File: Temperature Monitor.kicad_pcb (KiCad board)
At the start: 2 copper layers, 60 x 60 mm, 11 parts, among them J1 Battery, J2 BME 280, J3 Display, SW1 Up, SW2 Down, SW3 Select, U2 XIAO-ESP32-C6-SMD

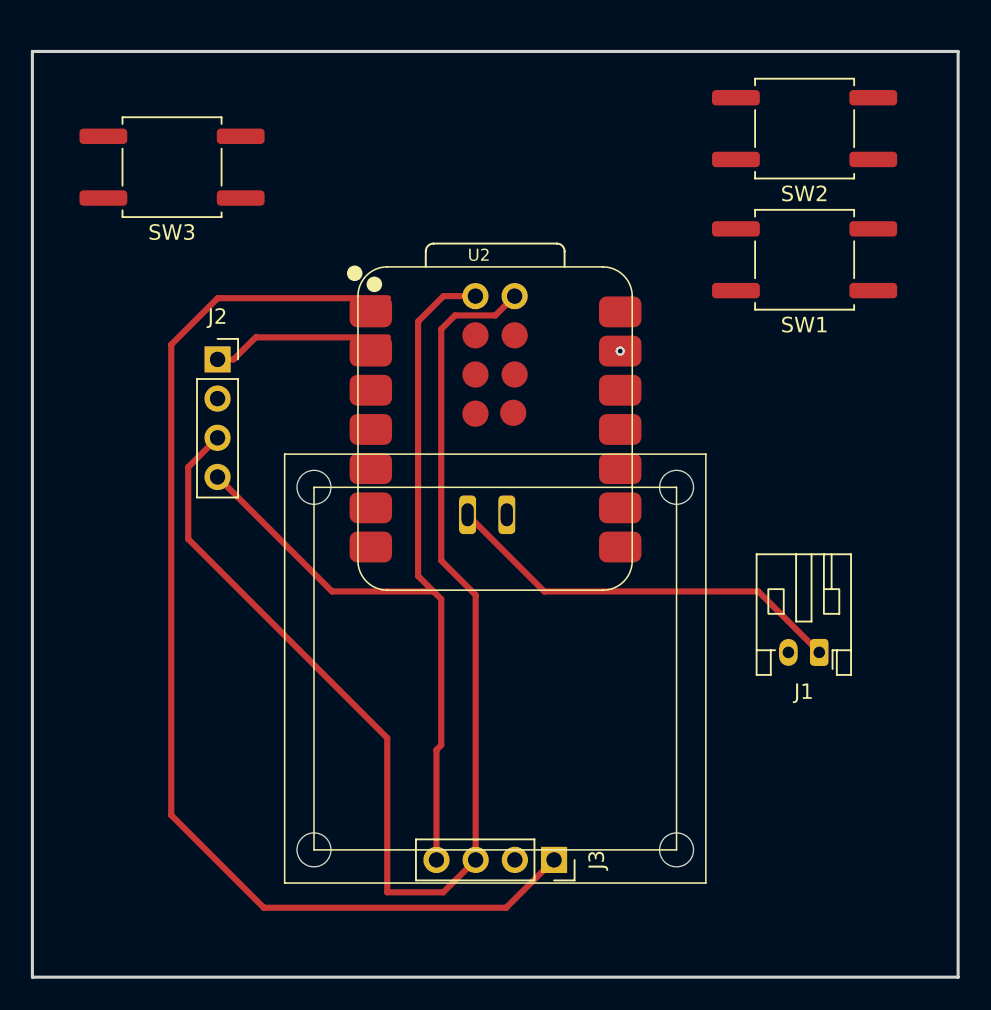
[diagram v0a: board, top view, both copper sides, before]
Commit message: Added buttons
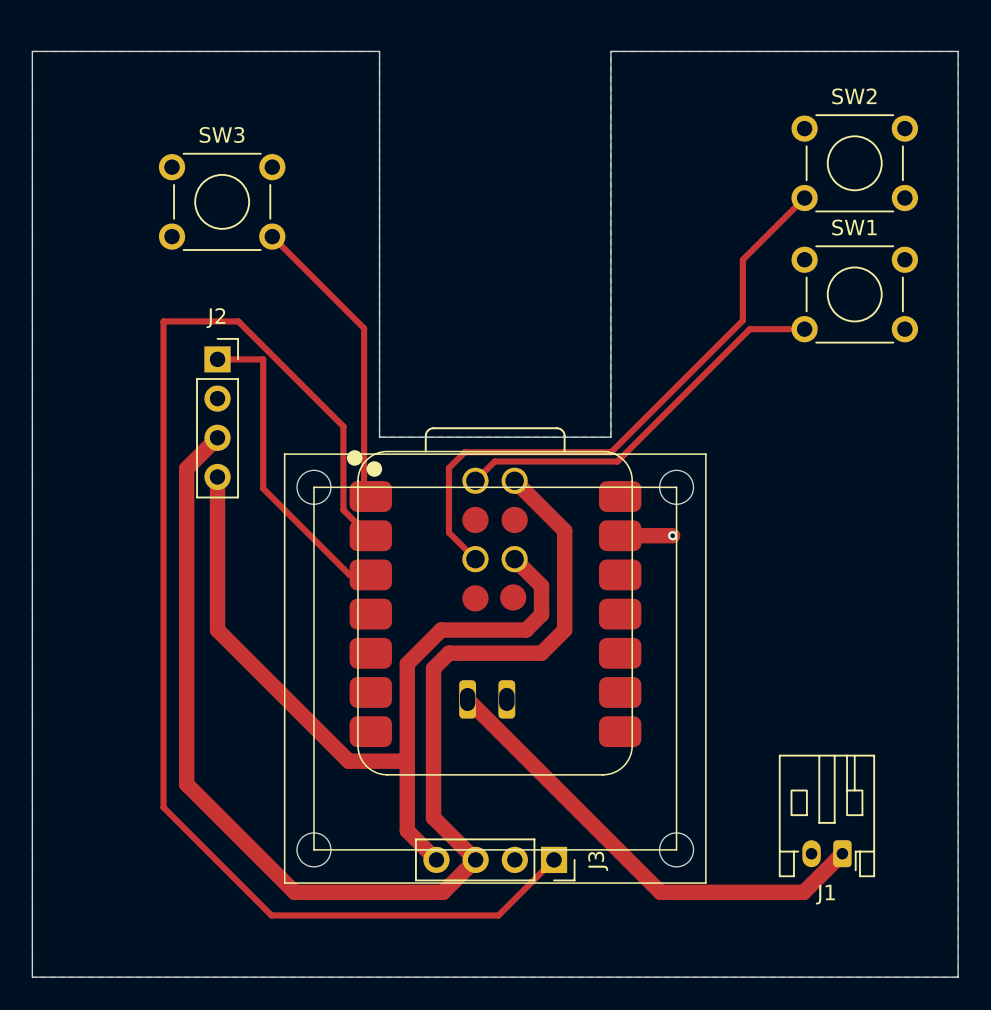
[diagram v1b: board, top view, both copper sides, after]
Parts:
- SW1: footprint Button_Switch_SMD:SW_Push_1P1T_NO_CK_KSC6xxG -> Button_Switch_THT:SW_TH_Tactile_Omron_B3F-100x
- SW2: footprint Button_Switch_SMD:SW_Push_1P1T_NO_CK_KSC6xxG -> Button_Switch_THT:SW_TH_Tactile_Omron_B3F-102x
- SW3: footprint Button_Switch_SMD:SW_Push_1P1T_NO_CK_KSC6xxG -> Button_Switch_THT:SW_TH_Tactile_Omron_B3F-106x
- moved J1 13.1 mm to (162.5, 127.0)
- moved U2 12.0 mm to (131.1, 122.0)
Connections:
- net Net-(J1-Pin_1) renamed /VBAT
- net Net-(J2-Pin_3) renamed /SCL
- J2 pad 1: Net-(J2-Pin_1) -> /SENS_PWR
- J2 pad 4: Net-(J2-Pin_4) -> /SDA
- J3 pad 1: Net-(J3-Pin_1) -> /DISP_PWR
- J3 pad 4: Net-(J2-Pin_4) -> /SDA
- SW1 pad 1: unconnected-(SW1-Pad1) -> GND
- SW1 pad 2: unconnected-(SW1-Pad2) -> Net-(U2-MTDI)
- SW2 pad 1: unconnected-(SW2-Pad1) -> GND
- SW2 pad 2: unconnected-(SW2-Pad2) -> Net-(U2-MTMS)
- SW3 pad 1: unconnected-(SW3-Pad1) -> GND
- SW3 pad 2: unconnected-(SW3-Pad2) -> Net-(U2-D0)
- U2 pad 1: Net-(J3-Pin_1) -> Net-(U2-D0)
- U2 pad 15: Net-(J2-Pin_4) -> Net-(U2-MTDI)
- U2 pad 19: unconnected-(U2-MTMS-Pad19) -> Net-(U2-MTMS)
- U2 pad 2: Net-(J2-Pin_1) -> /DISP_PWR
- U2 pad 20: unconnected-(U2-MTCK-Pad20) -> /SDA
- U2 pad 3: unconnected-(U2-D2-Pad3) -> /SENS_PWR
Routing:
- net /DISP_PWR: track 0.00 -> 83.7 mm
- net Net-(J3-Pin_1): track 74.4 -> 0.00 mm
- net Net-(J2-Pin_4): track 57.1 -> 0.00 mm
- net /SDA: track 0.00 -> 53.6 mm
- net Net-(U2-MTMS): track 0.00 -> 39.2 mm
- net Net-(U2-MTDI): track 0.00 -> 25.4 mm
- net /SENS_PWR: track 0.00 -> 20.6 mm
- net Net-(U2-D0): track 0.00 -> 20.2 mm
- net Net-(J2-Pin_1): track 11.7 -> 0.00 mm
- net /VBAT: track 26.5 -> 30.5 mm
- net GND: track 0.00 -> 3.40 mm
- net /SCL: track 83.2 -> 79.9 mm
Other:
- outline, holes or cut-outs redrawn

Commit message: Added SCL resistor
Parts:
- added R1: 220R, Resistor_THT:R_Axial_DIN0207_L6.3mm_D2.5mm_P7.62mm_Horizontal, F.Cu at (131.1, 123.5)
- added R2: 220R, Resistor_THT:R_Axial_DIN0207_L6.3mm_D2.5mm_P7.62mm_Horizontal, F.Cu at (125.0, 109.0)
- added R3: 5K, Resistor_THT:R_Axial_DIN0207_L6.3mm_D2.5mm_P7.62mm_Horizontal, F.Cu at (148.5, 123.5)
- moved J2 7.18 mm to (126.0, 89.0)
- moved SW3 3.59 mm to (116.8, 79.8)
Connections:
- U2 pad 12: unconnected-(U2-3V3_OUT-Pad12) -> /SENS_PWR
- U2 pad 3: /SENS_PWR -> Net-(U2-D2)
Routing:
- net /SDA: track 53.6 -> 82.1 mm
- net Net-(U2-D2): track 0.00 -> 22.7 mm
- net /SCL: track 79.9 -> 98.4 mm
- net /DISP_PWR: track 83.7 -> 73.9 mm
- net /VBAT: track 30.5 -> 38.8 mm
- net Net-(U2-MTDI): track 25.4 -> 29.8 mm
- net /SENS_PWR: track 20.6 -> 16.7 mm
- net Net-(U2-D0): track 20.2 -> 23.9 mm
- net Net-(U2-MTMS): track 39.2 -> 42.2 mm

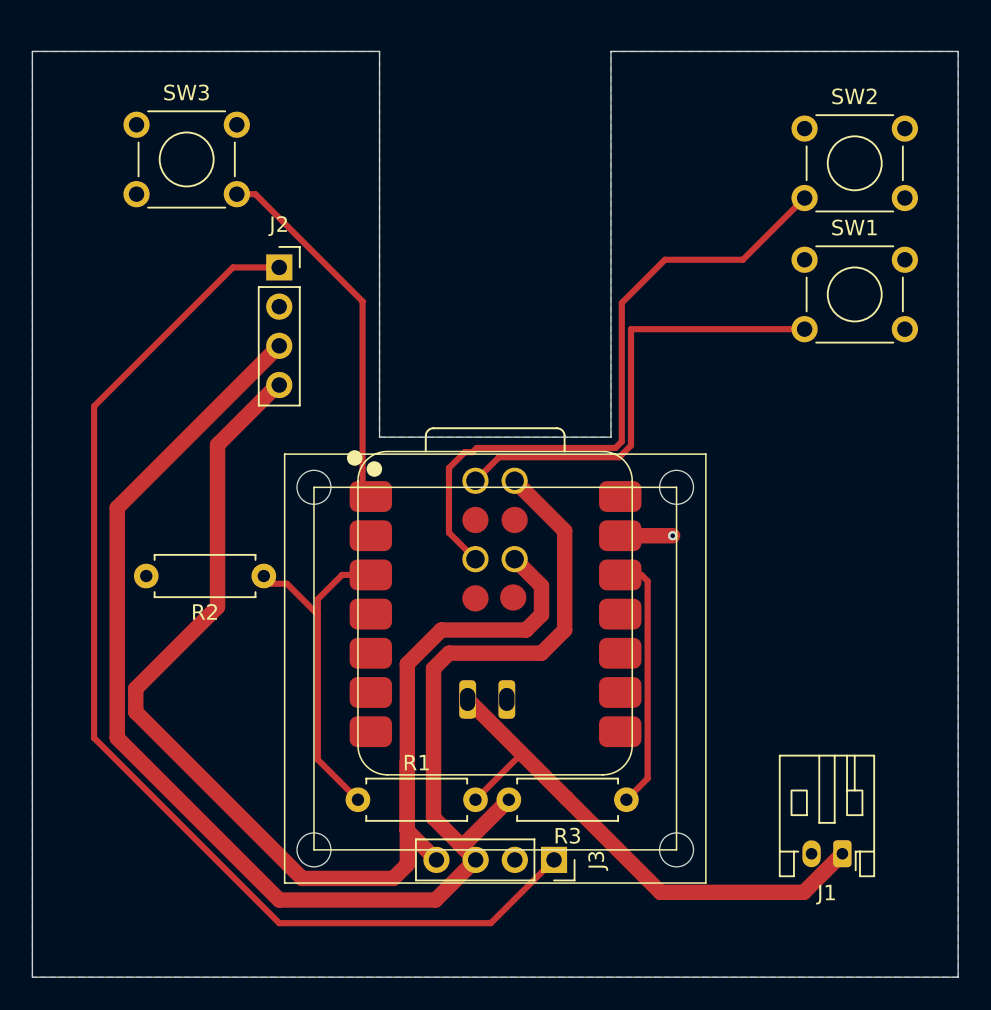
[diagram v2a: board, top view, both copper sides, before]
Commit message: Added Underside Traces
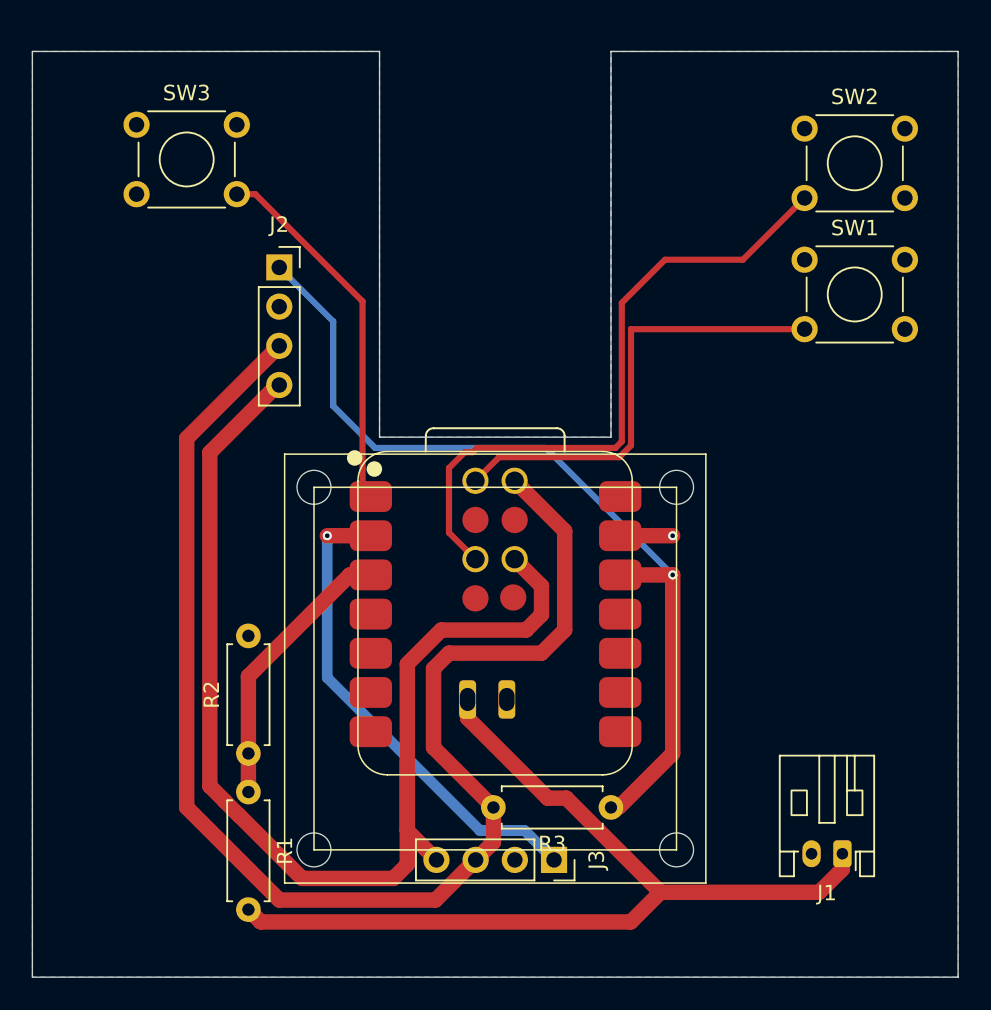
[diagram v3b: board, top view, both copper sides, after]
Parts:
- moved R2 11.5 mm to (124.0, 120.5), turned to 90 degrees
- moved R1 7.12 mm to (124.0, 123.0), turned to -90 degrees
- moved R3 1.12 mm to (147.5, 124.0)
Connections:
- net Net-(U2-D2) renamed /BATT_V
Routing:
- net /DISP_PWR: track 73.9 -> 31.8 mm, vias 0 -> 1
- net /SENS_PWR: track 16.7 -> 57.4 mm, vias 0 -> 1
- net /VBAT: track 38.8 -> 62.9 mm
- net /SCL: track 98.4 -> 89.7 mm
- net /BATT_V: track 22.7 -> 18.2 mm
- net /SDA: track 82.1 -> 78.1 mm

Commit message: Updated to match SMB circuit
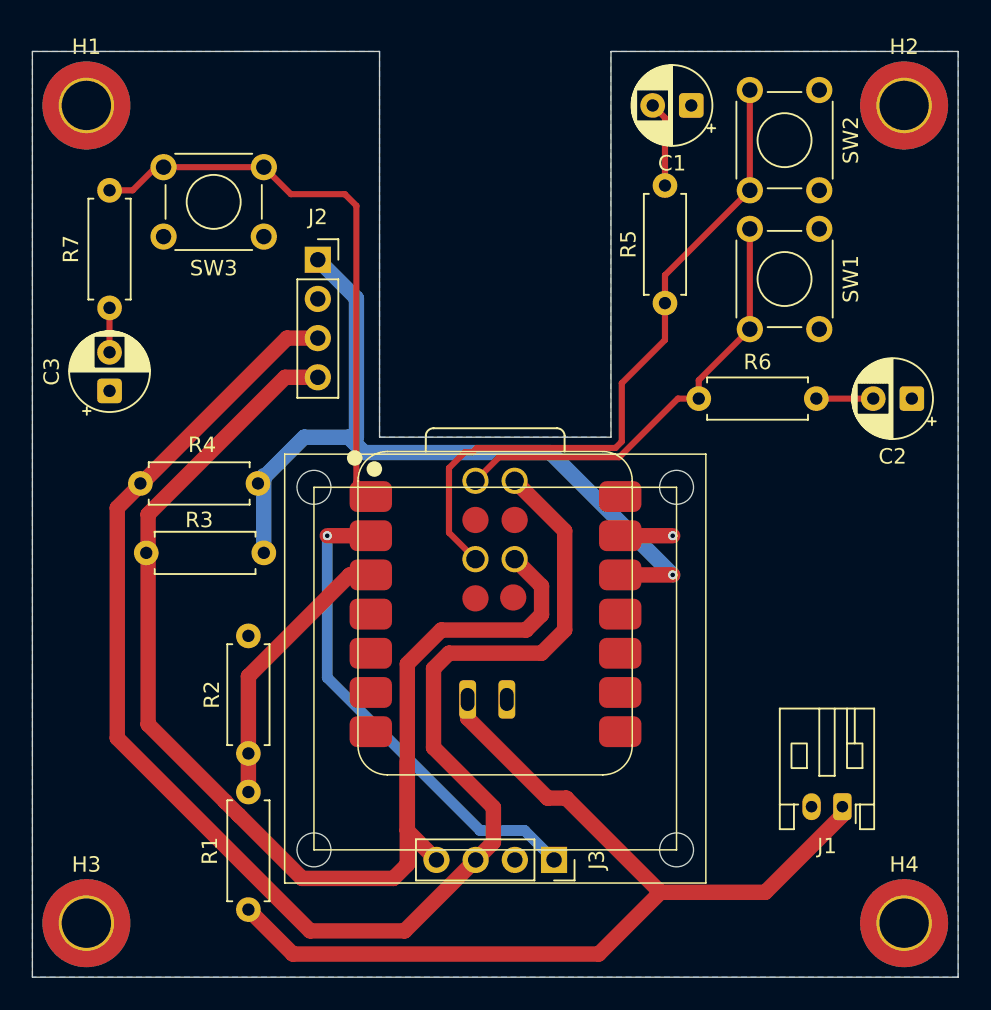
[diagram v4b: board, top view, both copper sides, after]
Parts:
- added C1: 0.1, Capacitor_THT:CP_Radial_D5.0mm_P2.50mm, F.Cu at (152.7, 78.5)
- added C2: 0.1, Capacitor_THT:CP_Radial_D5.0mm_P2.50mm, F.Cu at (167.0, 97.5)
- added C3: 0.1, Capacitor_THT:CP_Radial_D5.0mm_P2.50mm, F.Cu at (115.0, 97.0)
- added H1: MountingHole_Pad, MountingHole:MountingHole_3.2mm_M3_ISO7380_Pad_TopBottom, F.Cu at (113.5, 78.5)
- added H2: MountingHole_Pad, MountingHole:MountingHole_3.2mm_M3_ISO7380_Pad_TopBottom, F.Cu at (166.5, 78.5)
- added H3: MountingHole_Pad, MountingHole:MountingHole_3.2mm_M3_ISO7380_Pad_TopBottom, F.Cu at (113.5, 131.5)
- added H4: MountingHole_Pad, MountingHole:MountingHole_3.2mm_M3_ISO7380_Pad_TopBottom, F.Cu at (166.5, 131.5)
- added R4: 5K, Resistor_THT:R_Axial_DIN0207_L6.3mm_D2.5mm_P7.62mm_Horizontal, F.Cu at (117.4, 107.5)
- added R5: 1K, Resistor_THT:R_Axial_DIN0207_L6.3mm_D2.5mm_P7.62mm_Horizontal, F.Cu at (151.0, 91.3)
- added R6: 1K, Resistor_THT:R_Axial_DIN0207_L6.3mm_D2.5mm_P7.62mm_Horizontal, F.Cu at (153.2, 97.5)
- added R7: 1K, Resistor_THT:R_Axial_DIN0207_L6.3mm_D2.5mm_P7.62mm_Horizontal, F.Cu at (115.0, 84.0)
- moved R3 31.1 mm to (124.6, 103.0)
- moved SW3 11.0 mm to (125.0, 87.0), turned to 180 degrees
- moved J1 3.05 mm to (162.5, 124.0)
- moved SW2 2.67 mm to (161.0, 77.5), turned to -90 degrees
- moved J2 2.55 mm to (128.5, 88.5)
- moved SW1 2.21 mm to (161.0, 86.5), turned to -90 degrees
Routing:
- net Net-(U2-D0): track 23.9 -> 36.4 mm
- net /SCL: track 89.7 -> 97.8 mm
- net /SDA: track 78.1 -> 84.1 mm
- net Net-(C1-Pad2): track 0.00 -> 5.52 mm
- net /SENS_PWR: track 57.4 -> 53.1 mm
- net Net-(C2-Pad2): track 0.00 -> 3.69 mm
- net Net-(C3-Pad2): track 0.00 -> 2.88 mm
- net Net-(U2-MTMS): track 42.2 -> 44.8 mm
- net Net-(U2-MTDI): track 29.8 -> 29.1 mm
- net /VBAT: track 62.9 -> 62.4 mm

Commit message: General Improvements
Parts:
- C1, C2: value 0.1 -> 0.1U
- R1, R2: value 220R -> 220K
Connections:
- net Net-(U2-MTDI) renamed /Up
- net Net-(U2-MTMS) renamed /Down
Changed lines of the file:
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@@
 			)
 		)
-		(property "Value" "220R"
+		(property "Value" "220K"
 			(at 3.81 2.37 90)
 			(layer "F.Fab")
@@
 			(keep_end_layers yes)
 			(zone_layer_connections)
-			(net "Net-(U2-MTMS)")
+			(net "/Down")
 			(pinfunction "2_2")
 			(pintype "passive")
@@
 			(keep_end_layers yes)
 			(zone_layer_connections)
-			(net "Net-(U2-MTMS)")
+			(net "/Down")
 			(pinfunction "2_2")
 			(pintype "passive")
@@
 			(keep_end_layers yes)
 			(zone_layer_connections)
-			(net "Net-(U2-MTDI)")
+			(net "/Up")
 			(pintype "passive")
 		)
@@
 			)
 		)
-		(property "Value" "0.1"
+		(property "Value" "0.1U"
 			(at 1.25 3.75 0)
 			(layer "F.Fab")
@@
 			(keep_end_layers yes)
 			(zone_layer_connections)
-			(net "Net-(U2-MTDI)")
+			(net "/Up")
 			(pinfunction "MTDI_15")
 			(pintype "passive")
@@
 			(keep_end_layers yes)
 			(zone_layer_connections)
-			(net "Net-(U2-MTMS)")
+			(net "/Down")
 			(pinfunction "MTMS_19")
 			(pintype "passive")
@@
 			(keep_end_layers yes)
 			(zone_layer_connections)
-			(net "Net-(U2-MTMS)")
+			(net "/Down")
 			(pintype "passive")
 		)
@@
 			(keep_end_layers yes)
 			(zone_layer_connections)
-			(net "Net-(U2-MTDI)")
+			(net "/Up")
 			(pinfunction "2_2")
 			(pintype "passive")
@@
 			(keep_end_layers yes)
 			(zone_layer_connections)
-			(net "Net-(U2-MTDI)")
+			(net "/Up")
 			(pinfunction "2_2")
 			(pintype "passive")
@@
 			)
 		)
-		(property "Value" "0.1"
+		(property "Value" "0.1U"
 			(at 1.25 3.75 0)
 			(layer "F.Fab")
@@
 			)
 		)
-		(property "Value" "220R"
+		(property "Value" "220K"
 			(at 3.81 -0.5 90)
 			(layer "F.Fab")
@@
 	)
 	(segment
+		(start 115 91.62)
+		(end 115 94.5)
+		(width 0.4)
+		(layer "F.Cu")
+		(net "Net-(C3-Pad2)")
+	)
+	(segment
 		(start 157.5 129.5)
 		(end 162.5 124.5)
@@
 	)
 	(segment
-		(start 148.2 100.289949)
-		(end 148.2 96.5)
-		(width 0.4)
-		(layer "F.Cu")
-		(net "Net-(U2-MTMS)")
-	)
-	(segment
-		(start 151 91.31)
-		(end 151 93.7)
-		(width 0.4)
-		(layer "F.Cu")
-		(net "Net-(U2-MTMS)")
-	)
-	(segment
-		(start 138.7166 107.9068)
-		(end 137 106.1902)
-		(width 0.4)
-		(layer "F.Cu")
-		(net "Net-(U2-MTMS)")
-	)
-	(segment
-		(start 156.5 84)
-		(end 156.5 77.5)
-		(width 0.4)
-		(layer "F.Cu")
-		(net "Net-(U2-MTMS)")
-	)
-	(segment
-		(start 138.0232 100.9768)
-		(end 138.5232 100.9768)
-		(width 0.4)
-		(layer "F.Cu")
-		(net "Net-(U2-MTMS)")
-	)
-	(segment
-		(start 151 93.7)
-		(end 148.2 96.5)
-		(width 0.4)
-		(layer "F.Cu")
-		(net "Net-(U2-MTMS)")
-	)
-	(segment
-		(start 138.8 100.7)
-		(end 147.789949 100.7)
-		(width 0.4)
-		(layer "F.Cu")
-		(net "Net-(U2-MTMS)")
-	)
-	(segment
-		(start 137 106.1902)
-		(end 137 102)
-		(width 0.4)
-		(layer "F.Cu")
-		(net "Net-(U2-MTMS)")
-	)
-	(segment
-		(start 151 91.31)
-		(end 151 89.5)
-		(width 0.4)
-		(layer "F.Cu")
-		(net "Net-(U2-MTMS)")
-	)
-	(segment
-		(start 137 102)
-		(end 138.0232 100.9768)
-		(width 0.4)
-		(layer "F.Cu")
-		(net "Net-(U2-MTMS)")
-	)
-	(segment
-		(start 138.5232 100.9768)
-		(end 138.8 100.7)
-		(width 0.4)
-		(layer "F.Cu")
-		(net "Net-(U2-MTMS)")
-	)
-	(segment
-		(start 147.789949 100.7)
-		(end 148.2 100.289949)
-		(width 0.4)
-		(layer "F.Cu")
-		(net "Net-(U2-MTMS)")
-	)
-	(segment
-		(start 151 89.5)
-		(end 156.5 84)
-		(width 0.4)
-		(layer "F.Cu")
-		(net "Net-(U2-MTMS)")
-	)
-	(segment
 		(start 148.1 108.9283)
 		(end 151.5 108.9283)
@@
 	)
 	(segment
-		(start 153.19 96.31)
-		(end 156.5 93)
+		(start 160.81 97.5)
+		(end 164.5 97.5)
 		(width 0.4)
 		(layer "F.Cu")
-		(net "Net-(U2-MTDI)")
+		(net "Net-(C2-Pad2)")
 	)
 	(segment
-		(start 140.2434 101.3)
-		(end 148.038477 101.3)
+		(start 151 83.69)
+		(end 151 79.294887)
 		(width 0.4)
 		(layer "F.Cu")
-		(net "Net-(U2-MTDI)")
+		(net "Net-(C1-Pad2)")
 	)
 	(segment
-		(start 151.838477 97.5)
-		(end 153.19 97.5)
+		(start 151 79.294887)
+		(end 150.205113 78.5)
 		(width 0.4)
 		(layer "F.Cu")
-		(net "Net-(U2-MTDI)")
+		(net "Net-(C1-Pad2)")
 	)
 	(segment
-		(start 156.5 86.5)
-		(end 156.5 93)
+		(start 148.2 100.289949)
+		(end 148.2 96.5)
 		(width 0.4)
 		(layer "F.Cu")
-		(net "Net-(U2-MTDI)")
+		(net "/Down")
 	)
 	(segment
-		(start 153.19 97.5)
-		(end 153.19 96.31)
+		(start 151 91.31)
+		(end 151 93.7)
 		(width 0.4)
 		(layer "F.Cu")
-		(net "Net-(U2-MTDI)")
+		(net "/Down")
 	)
 	(segment
-		(start 138.7166 102.8268)
-		(end 140.2434 101.3)
+		(start 138.7166 107.9068)
+		(end 137 106.1902)
 		(width 0.4)
 		(layer "F.Cu")
-		(net "Net-(U2-MTDI)")
+		(net "/Down")
 	)
 	(segment
-		(start 148.038477 101.3)
-		(end 151.838477 97.5)
+		(start 156.5 84)
+		(end 156.5 77.5)
 		(width 0.4)
 		(layer "F.Cu")
-		(net "Net-(U2-MTDI)")
+		(net "/Down")
 	)
 	(segment
-		(start 151 83.69)
-		(end 151 79.294887)
+		(start 138.0232 100.9768)
+		(end 138.5232 100.9768)
 		(width 0.4)
 		(layer "F.Cu")
-		(net "Net-(C1-Pad2)")
+		(net "/Down")
 	)
 	(segment
-		(start 151 79.294887)
-		(end 150.205113 78.5)
+		(start 151 93.7)
+		(end 148.2 96.5)
 		(width 0.4)
 		(layer "F.Cu")
-		(net "Net-(C1-Pad2)")
+		(net "/Down")
 	)
 	(segment
-		(start 160.81 97.5)
-		(end 164.5 97.5)
+		(start 138.8 100.7)
+		(end 147.789949 100.7)
 		(width 0.4)
 		(layer "F.Cu")
-		(net "Net-(C2-Pad2)")
+		(net "/Down")
 	)
 	(segment
-		(start 115 91.62)
-		(end 115 94.5)
+		(start 137 106.1902)
+		(end 137 102)
 		(width 0.4)
 		(layer "F.Cu")
-		(net "Net-(C3-Pad2)")
+		(net "/Down")
+	)
+	(segment
+		(start 151 91.31)
+		(end 151 89.5)
+		(width 0.4)
+		(layer "F.Cu")
+		(net "/Down")
+	)
+	(segment
+		(start 137 102)
+		(end 138.0232 100.9768)
+		(width 0.4)
+		(layer "F.Cu")
+		(net "/Down")
+	)
+	(segment
+		(start 138.5232 100.9768)
+		(end 138.8 100.7)
+		(width 0.4)
+		(layer "F.Cu")
+		(net "/Down")
+	)
+	(segment
+		(start 147.789949 100.7)
+		(end 148.2 100.289949)
+		(width 0.4)
+		(layer "F.Cu")
+		(net "/Down")
+	)
+	(segment
+		(start 151 89.5)
+		(end 156.5 84)
+		(width 0.4)
+		(layer "F.Cu")
+		(net "/Down")
+	)
+	(segment
+		(start 153.19 96.31)
+		(end 156.5 93)
+		(width 0.4)
+		(layer "F.Cu")
+		(net "/Up")
+	)
+	(segment
+		(start 140.2434 101.3)
+		(end 148.038477 101.3)
+		(width 0.4)
+		(layer "F.Cu")
+		(net "/Up")
+	)
+	(segment
+		(start 151.838477 97.5)
+		(end 153.19 97.5)
+		(width 0.4)
+		(layer "F.Cu")
+		(net "/Up")
+	)
+	(segment
+		(start 156.5 86.5)
+		(end 156.5 93)
+		(width 0.4)
+		(layer "F.Cu")
+		(net "/Up")
+	)
+	(segment
+		(start 153.19 97.5)
+		(end 153.19 96.31)
+		(width 0.4)
+		(layer "F.Cu")
+		(net "/Up")
+	)
+	(segment
+		(start 138.7166 102.8268)
+		(end 140.2434 101.3)
+		(width 0.4)
+		(layer "F.Cu")
+		(net "/Up")
+	)
+	(segment
+		(start 148.038477 101.3)
+		(end 151.838477 97.5)
+		(width 0.4)
+		(layer "F.Cu")
+		(net "/Up")
 	)
 	(zone
